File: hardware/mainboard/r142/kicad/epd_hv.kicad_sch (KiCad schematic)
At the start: 33 parts, among them J3 FH34SRJ-24S-0.5SH(50), Q1 IRLML6346TRPBF

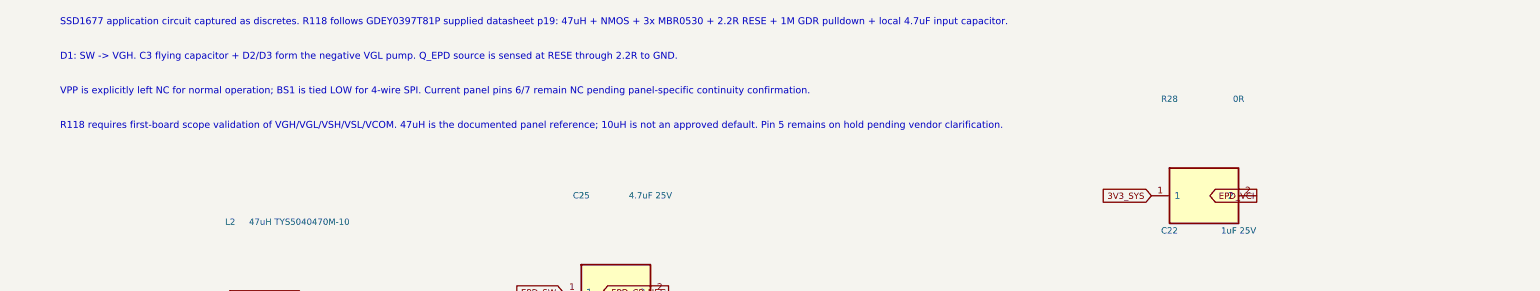
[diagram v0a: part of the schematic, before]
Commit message: R142: separate SD schematic group and refresh engineering notes; preserve electrical graph
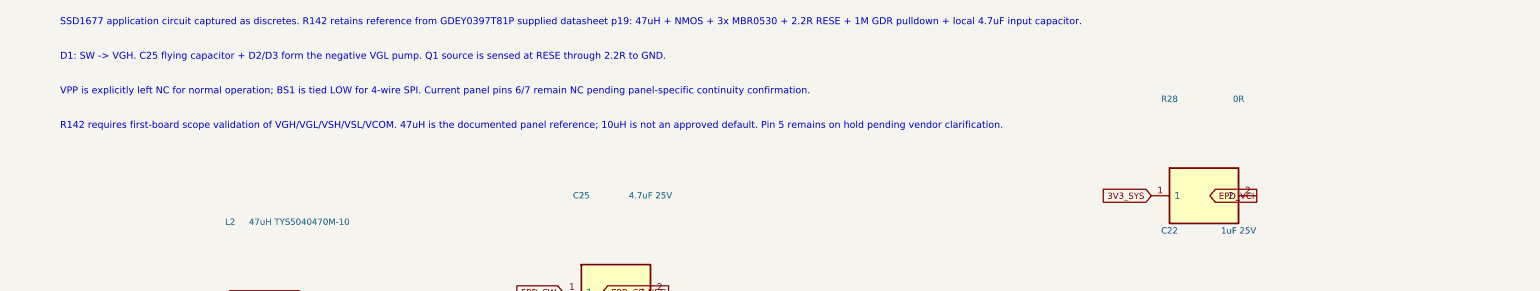
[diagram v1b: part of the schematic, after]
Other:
- note added: "D1: SW -> VGH. C25 flying capacitor + D2/D3 form the negative VGL pump. Q1 source is sensed at RESE through 2.2R to GND."
- note added: "R142 requires first-board scope validation of VGH/VGL/VSH/VSL/VCOM. 47uH is the documented panel reference; 10uH is not an approved default. Pin 5 remains on hold pending vendor clarification."
- note added: "SSD1677 application circuit captured as discretes. R142 retains reference from GDEY0397T81P supplied datasheet p19: 47uH + NMOS + 3x MBR0530 + 2.2R RESE + 1M GDR pulldown + local 4.7uF input capacitor."
- note removed: "D1: SW -> VGH. C3 flying capacitor + D2/D3 form the negative VGL pump. Q_EPD source is sensed at RESE through 2.2R to GND."
- note removed: "R118 requires first-board scope validation of VGH/VGL/VSH/VSL/VCOM. 47uH is the documented panel reference; 10uH is not an approved default. Pin 5 remains on hold pending vendor clarification."
- note removed: "SSD1677 application circuit captured as discretes. R118 follows GDEY0397T81P supplied datasheet p19: 47uH + NMOS + 3x MBR0530 + 2.2R RESE + 1M GDR pulldown + local 4.7uF input capacitor."
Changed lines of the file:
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@@
 	(global_label "GND" (shape input) (at 208.28 102.87 0) (effects (font (size 0.9 0.9)) (justify right bottom)))
 	(global_label "GND" (shape input) (at 247.65 102.87 180) (effects (font (size 0.9 0.9)) (justify right bottom)))
-	(text "SSD1677 application circuit captured as discretes. R118 follows GDEY0397T81P supplied datasheet p19: 47uH + NMOS + 3x MBR0530 + 2.2R RESE + 1M GDR pulldown + local 4.7uF input capacitor." (exclude_from_sim no) (at 25 20 0) (effects (font (size 1.0 1.0)) (justify left bottom)))
-	(text "D1: SW -> VGH. C3 flying capacitor + D2/D3 form the negative VGL pump. Q_EPD source is sensed at RESE through 2.2R to GND." (exclude_from_sim no) (at 25 25 0) (effects (font (size 1.0 1.0)) (justify left bottom)))
+	(text "SSD1677 application circuit captured as discretes. R142 retains reference from GDEY0397T81P supplied datasheet p19: 47uH + NMOS + 3x MBR0530 + 2.2R RESE + 1M GDR pulldown + local 4.7uF input capacitor." (exclude_from_sim no) (at 25 20 0) (effects (font (size 1.0 1.0)) (justify left bottom)))
+	(text "D1: SW -> VGH. C25 flying capacitor + D2/D3 form the negative VGL pump. Q1 source is sensed at RESE through 2.2R to GND." (exclude_from_sim no) (at 25 25 0) (effects (font (size 1.0 1.0)) (justify left bottom)))
 	(text "VPP is explicitly left NC for normal operation; BS1 is tied LOW for 4-wire SPI. Current panel pins 6/7 remain NC pending panel-specific continuity confirmation." (exclude_from_sim no) (at 25 30 0) (effects (font (size 1.0 1.0)) (justify left bottom)))
-	(text "R118 requires first-board scope validation of VGH/VGL/VSH/VSL/VCOM. 47uH is the documented panel reference; 10uH is not an approved default. Pin 5 remains on hold pending vendor clarification." (exclude_from_sim no) (at 25 35 0) (effects (font (size 1.0 1.0)) (justify left bottom)))
+	(text "R142 requires first-board scope validation of VGH/VGL/VSH/VSL/VCOM. 47uH is the documented panel reference; 10uH is not an approved default. Pin 5 remains on hold pending vendor clarification." (exclude_from_sim no) (at 25 35 0) (effects (font (size 1.0 1.0)) (justify left bottom)))
 	(symbol (lib_id "ENKU:TESTPOINT") (at 44.45 199.39 0) (unit 1) (exclude_from_sim no) (in_bom no) (on_board yes) (dnp no)
 		(property "Reference" "TP9" (at 44.45 196.85 0) (effects (font (size 0.9 0.9))))
